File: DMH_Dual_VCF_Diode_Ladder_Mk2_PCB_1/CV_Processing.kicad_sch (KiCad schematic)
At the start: 50 parts, among them J15 Conn_01x08_PinHeader, J16 Conn_01x08_PinHeader, SW10 SW_DPDT_OnOn, SW7 SW_SPDT_OnOffOn, SW9 SW_SPDT_OnOffOn, U7 TL074, U8 TL074

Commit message: validation ongoing
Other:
- note added: "Update cutoff pots limiting resistors"
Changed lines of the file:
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@@
 		(comment 1 "PCB for 15cm Kosmo format synthesizer module")
+	)
+	(text "Update cutoff pots limiting resistors"
+		(exclude_from_sim no)
+		(at 76.962 33.02 0)
+		(effects
+			(font
+				(size 1.27 1.27)
+			)
+		)
 	)
 	(junction

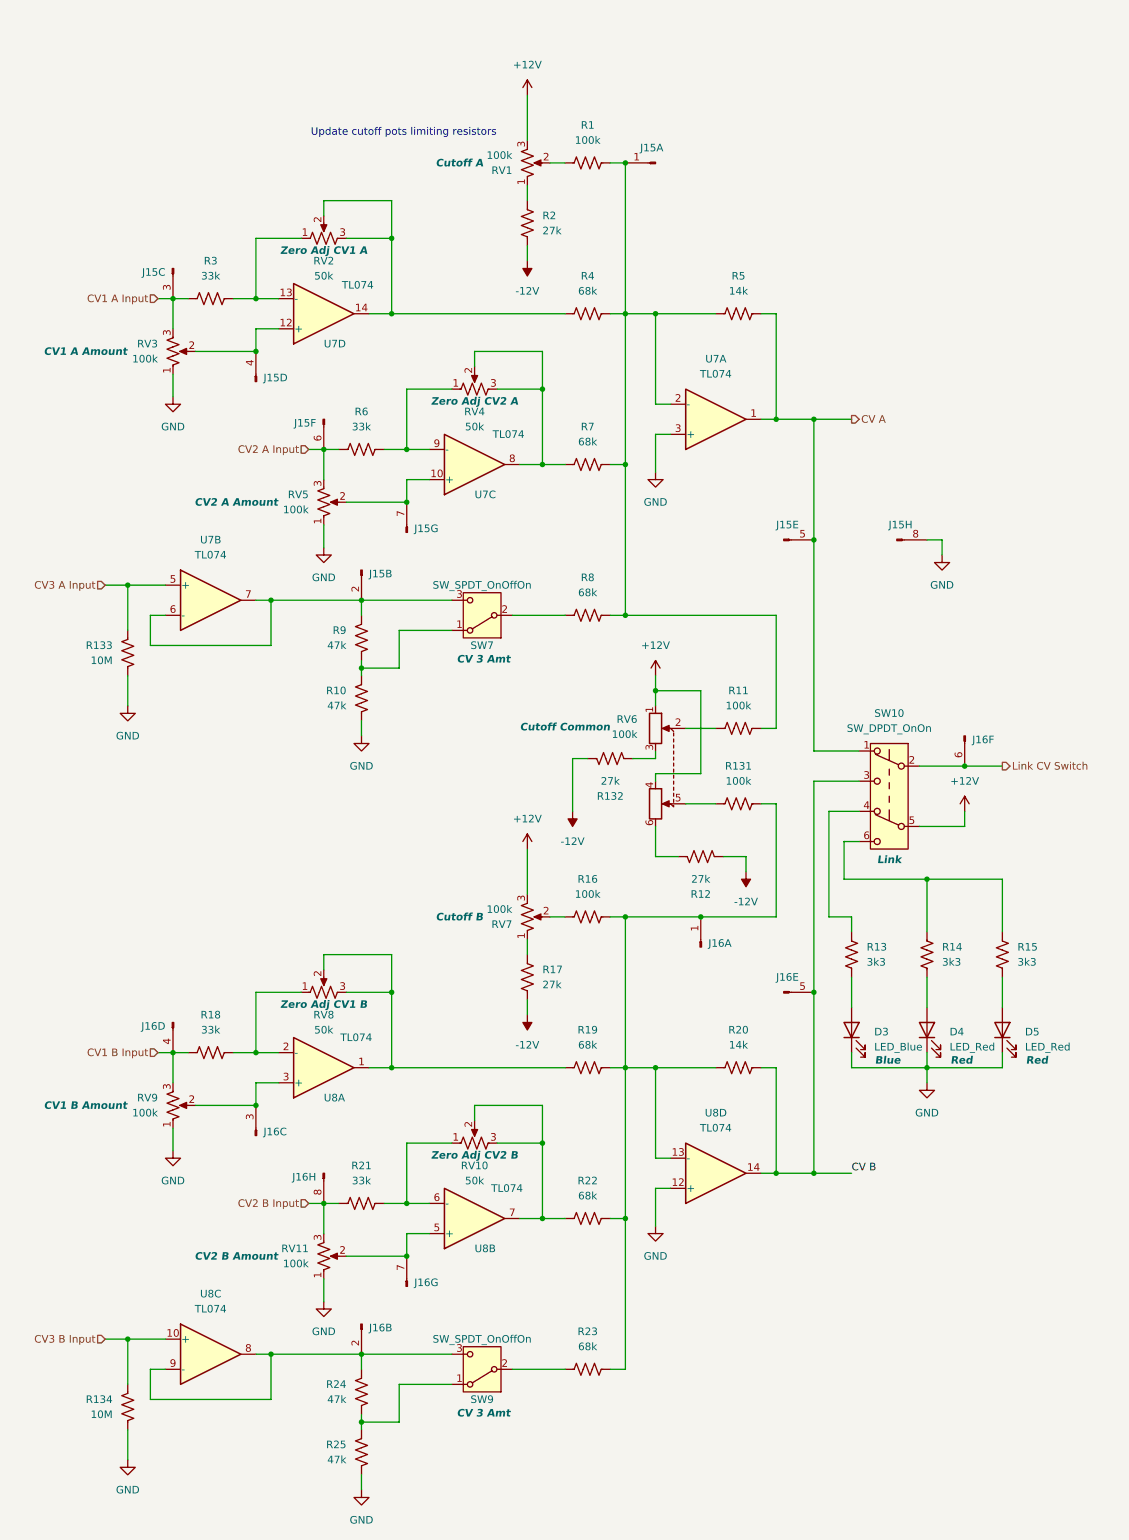
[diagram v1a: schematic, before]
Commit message: Updated schematic during validation
- Changed Resonance B VCA gain resistors to 2k2
- Added range limiting resistors to all Cutoff pots
- Moved 48x gain to non-inverting opamp stage in Core Circuit to allow for Resonance voltage control.
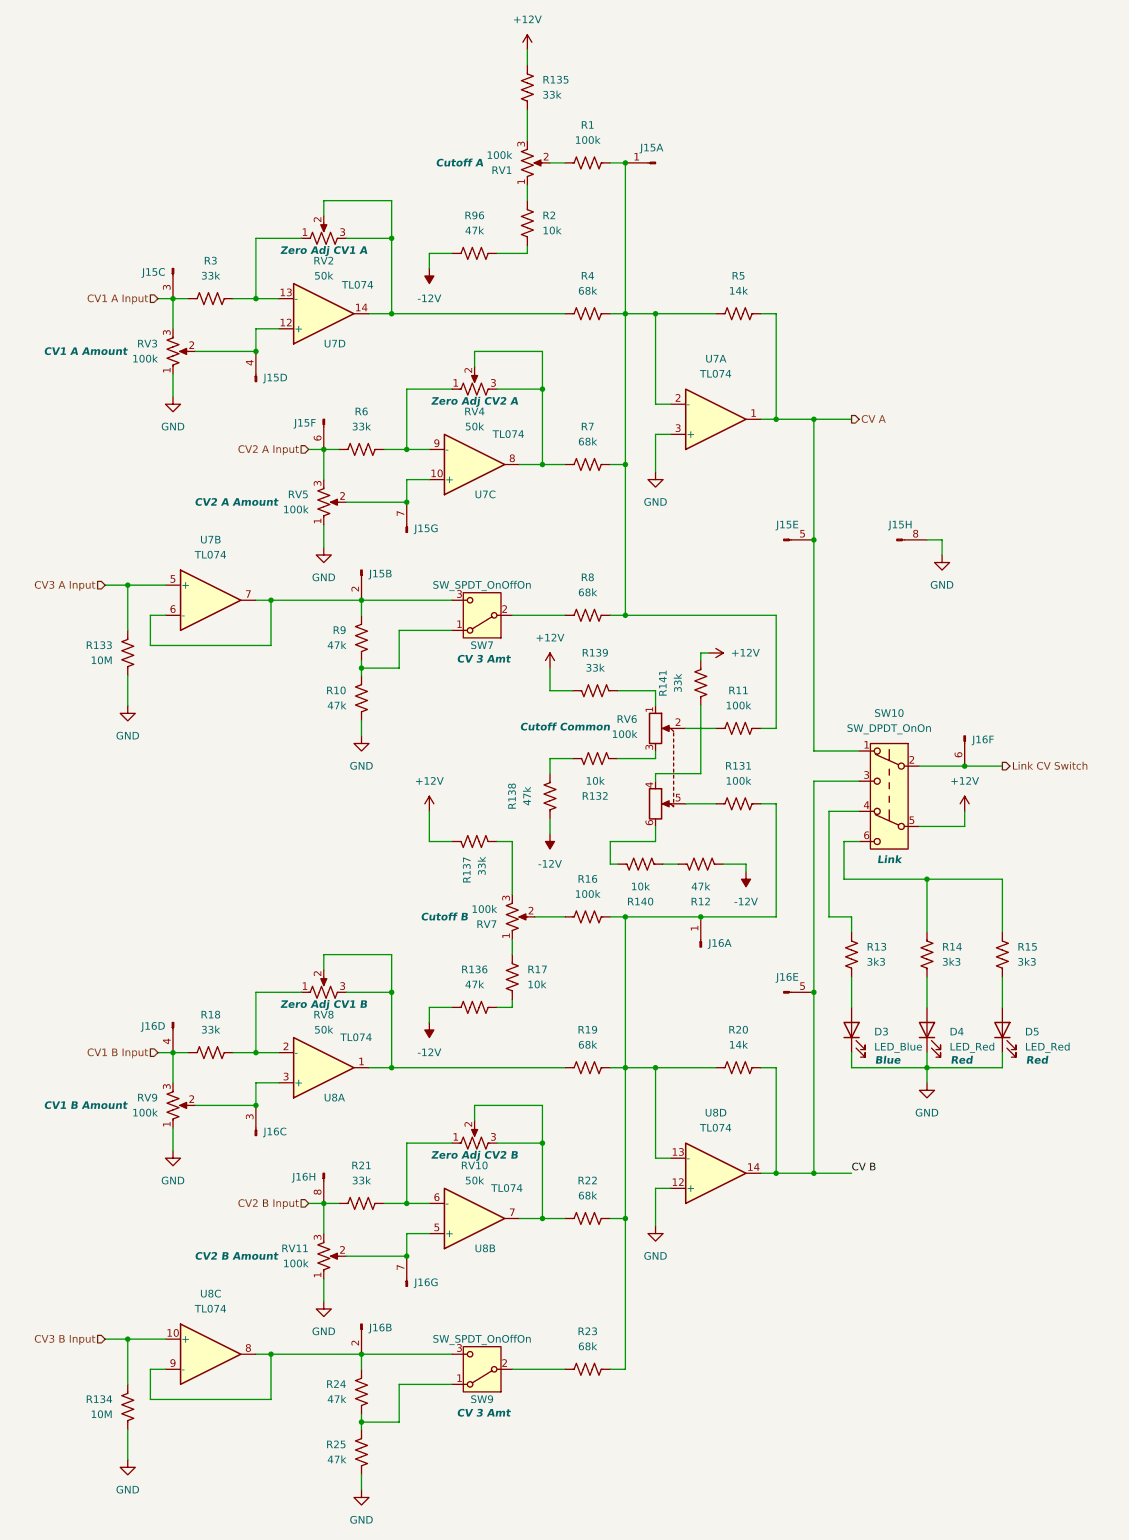
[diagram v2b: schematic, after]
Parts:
- added R135, R137, R139, R141: 33k, Resistor_THT:R_Axial_DIN0207_L6.3mm_D2.5mm_P7.62mm_Horizontal, symbol Device:R_US
- added R136, R138, R96: 47k, Resistor_THT:R_Axial_DIN0207_L6.3mm_D2.5mm_P7.62mm_Horizontal, symbol Device:R_US
- added R140: 10k, Resistor_THT:R_Axial_DIN0207_L6.3mm_D2.5mm_P7.62mm_Horizontal, symbol Device:R_US
- R12: value 27k -> 47k
- R132, R17, R2: value 27k -> 10k
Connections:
- net +12V: now also R135.2, R137.1, R139.1, R141.2; no longer RV1.3, RV6.1, RV6.4, RV7.3
- net -12V: now also R136.1, R138.1, R96.1; no longer R132.2, R17.2, R2.2
- net at R12.2: now also R140.1; no longer RV6.6
- new net: R139.2, RV6.1
- new net: R136.2, R17.2
- new net: R2.2, R96.2
- new net: R137.2, RV7.3
- new net: R141.1, RV6.4
- new net: R135.1, RV1.3
- new net: R140.2, RV6.6
- new net: R132.2, R138.2
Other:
- note removed: "Update cutoff pots limiting resistors"
- moved on the sheet: R12, R132, R17, RV7

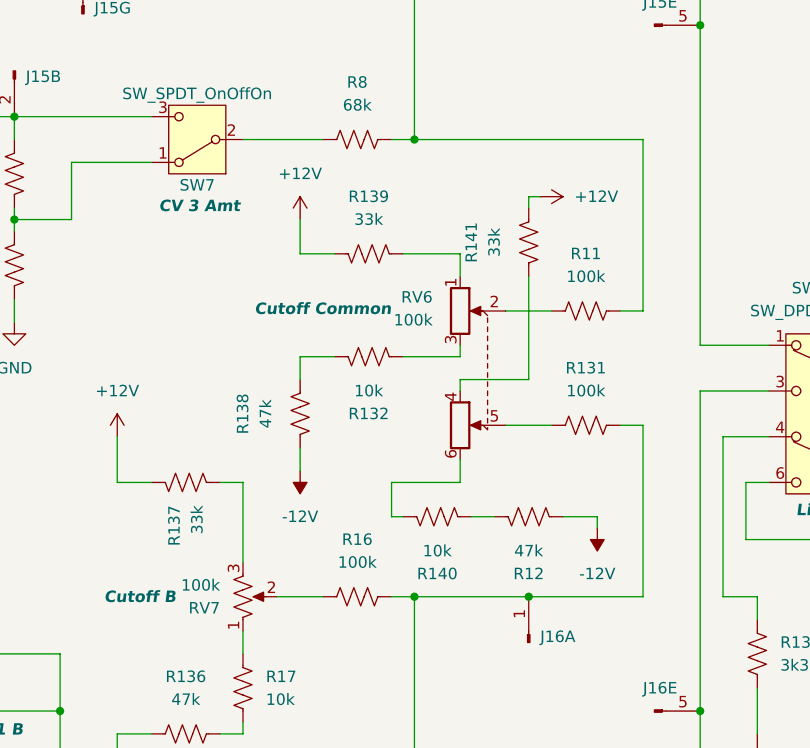
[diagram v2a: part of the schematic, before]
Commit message: Corrected polarization of dual pot in PCB 1 sch
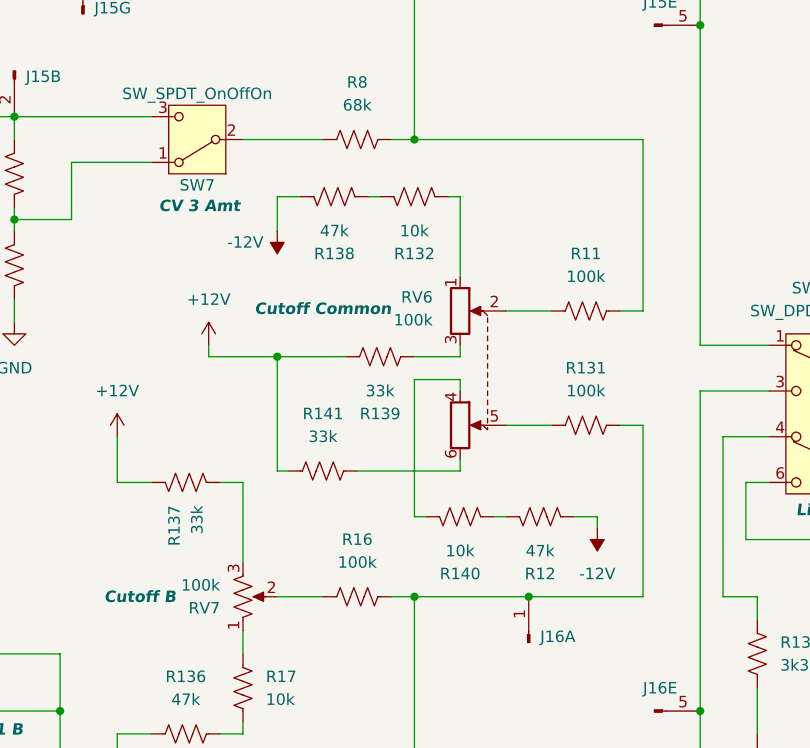
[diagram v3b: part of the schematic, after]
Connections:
- net -12V: now also R138.2; no longer R138.1
- net at R139.2: now also RV6.3; no longer RV6.1
- net at R141.1: now also RV6.6; no longer RV6.4
- net at R140.2: now also RV6.4; no longer RV6.6
- net at R132.1: now also RV6.1; no longer RV6.3
- net at R132.2: now also R138.1; no longer R138.2
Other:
- moved on the sheet: R12, R132, R138, R139, R140, R141

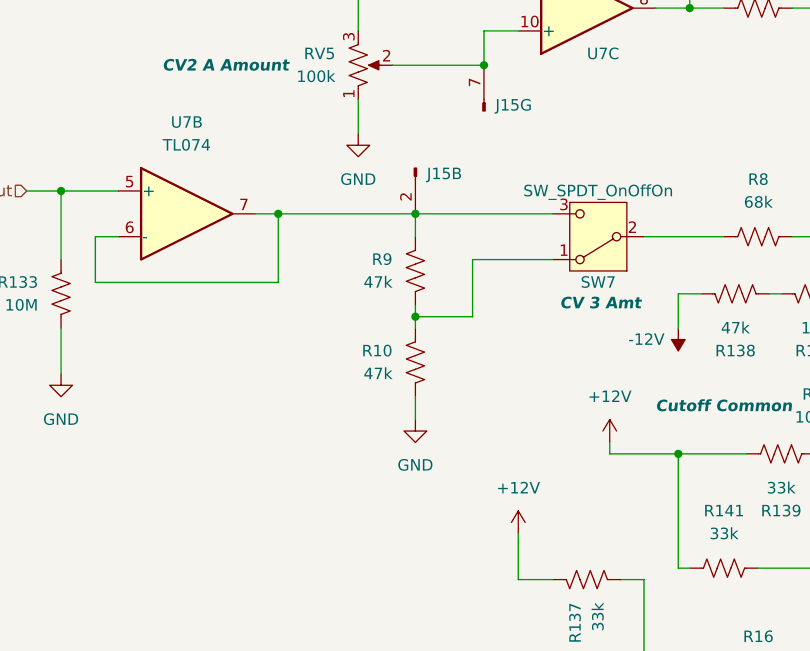
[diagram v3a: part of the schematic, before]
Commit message: Adapted CV3 A Input for V/Oct
Now need to repeat it for CV3 B
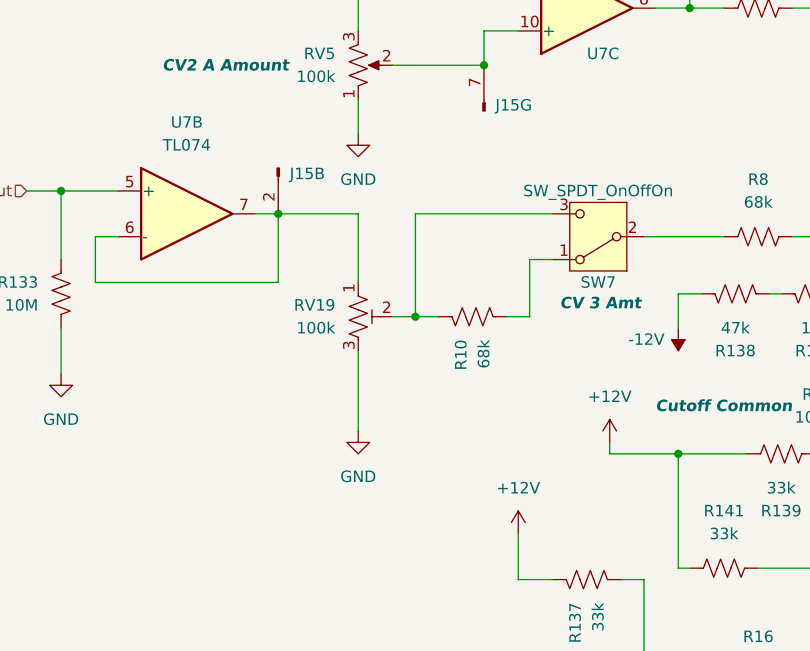
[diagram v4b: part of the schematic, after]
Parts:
- removed R9: 47k, Resistor_THT:R_Axial_DIN0207_L6.3mm_D2.5mm_P7.62mm_Horizontal, symbol Device:R_US
- added RV19: 100k, symbol Device:R_Potentiometer_Trim_US
- R10: value 47k -> 68k
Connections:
- net GND: now also RV19.3; no longer R10.1
- net at J15.2 (Pin_2), U7.6 (-), U7.7: now also RV19.1; no longer SW7.3 (C)
- net at SW7.1 (A): now also R10.1; no longer R10.2
- new net: R10.2, RV19.2, SW7.3 (C)
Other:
- moved on the sheet: R10

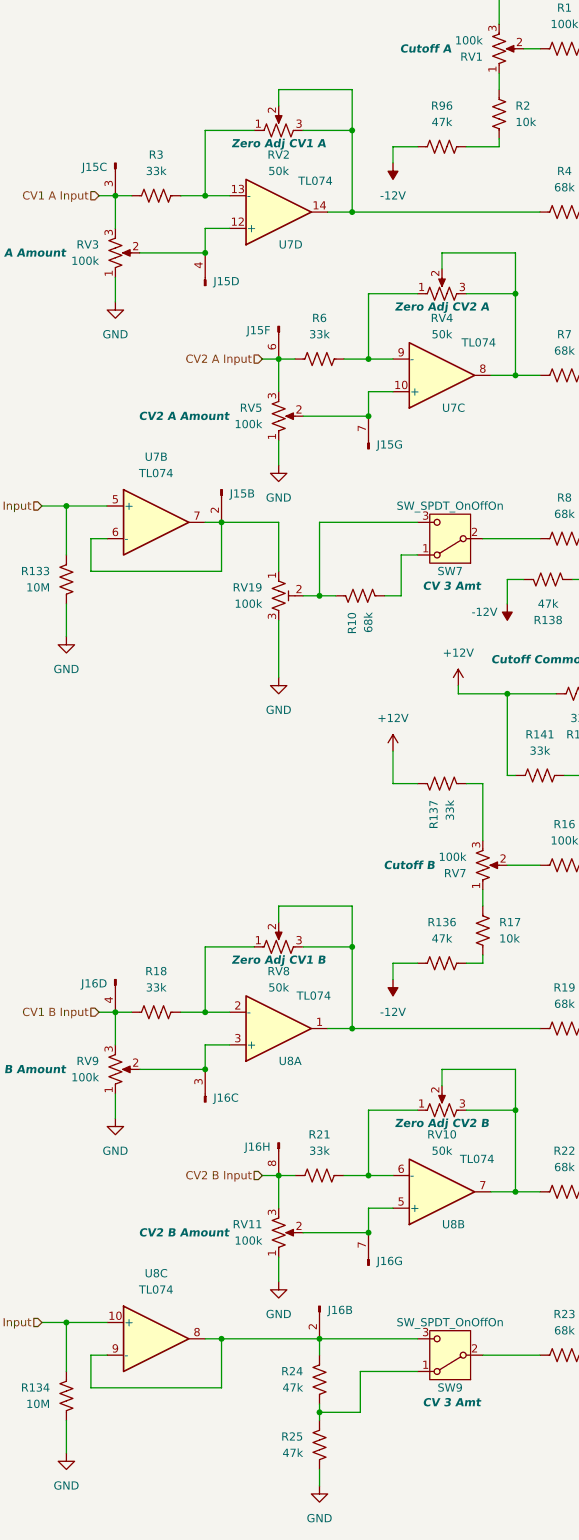
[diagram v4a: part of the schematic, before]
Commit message: Added V/oct calib to CV3 B
And changed output inverter stage resistors back to 100k
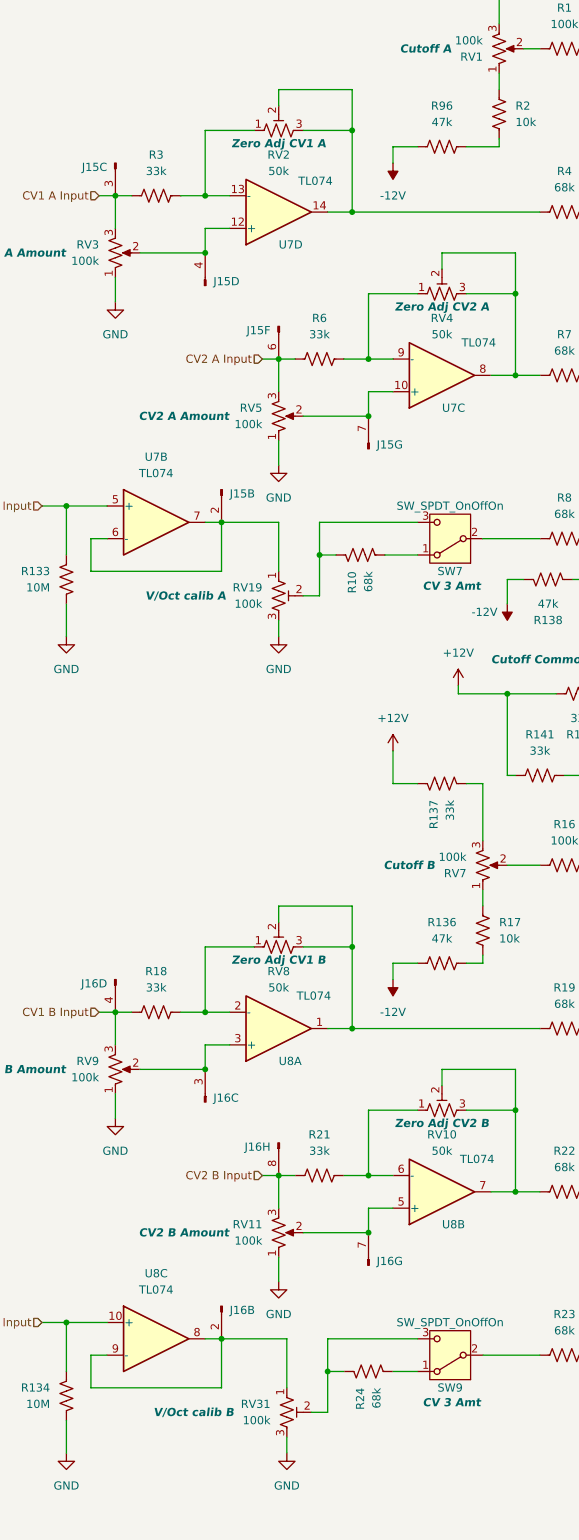
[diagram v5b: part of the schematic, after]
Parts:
- removed R25: 47k, Resistor_THT:R_Axial_DIN0207_L6.3mm_D2.5mm_P7.62mm_Horizontal, symbol Device:R_US
- added RV31: 100k, symbol Device:R_Potentiometer_Trim_US
- R24: value 47k -> 68k
- RV10, RV2, RV4, RV8: symbol Device:R_Potentiometer_US -> Device:R_Potentiometer_Trim_US
- RV19: Function (none) -> V/Oct calib A
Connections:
- net GND: now also RV31.3
- net at J16.2 (Pin_2), U8.8, U8.9 (-): now also RV31.1; no longer R24.2, SW9.3 (C)
- new net: R24.2, RV31.2, SW9.3 (C)
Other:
- moved on the sheet: R10, R24
